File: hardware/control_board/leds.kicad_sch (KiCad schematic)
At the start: 18 parts, among them Q1 PMV450ENEA

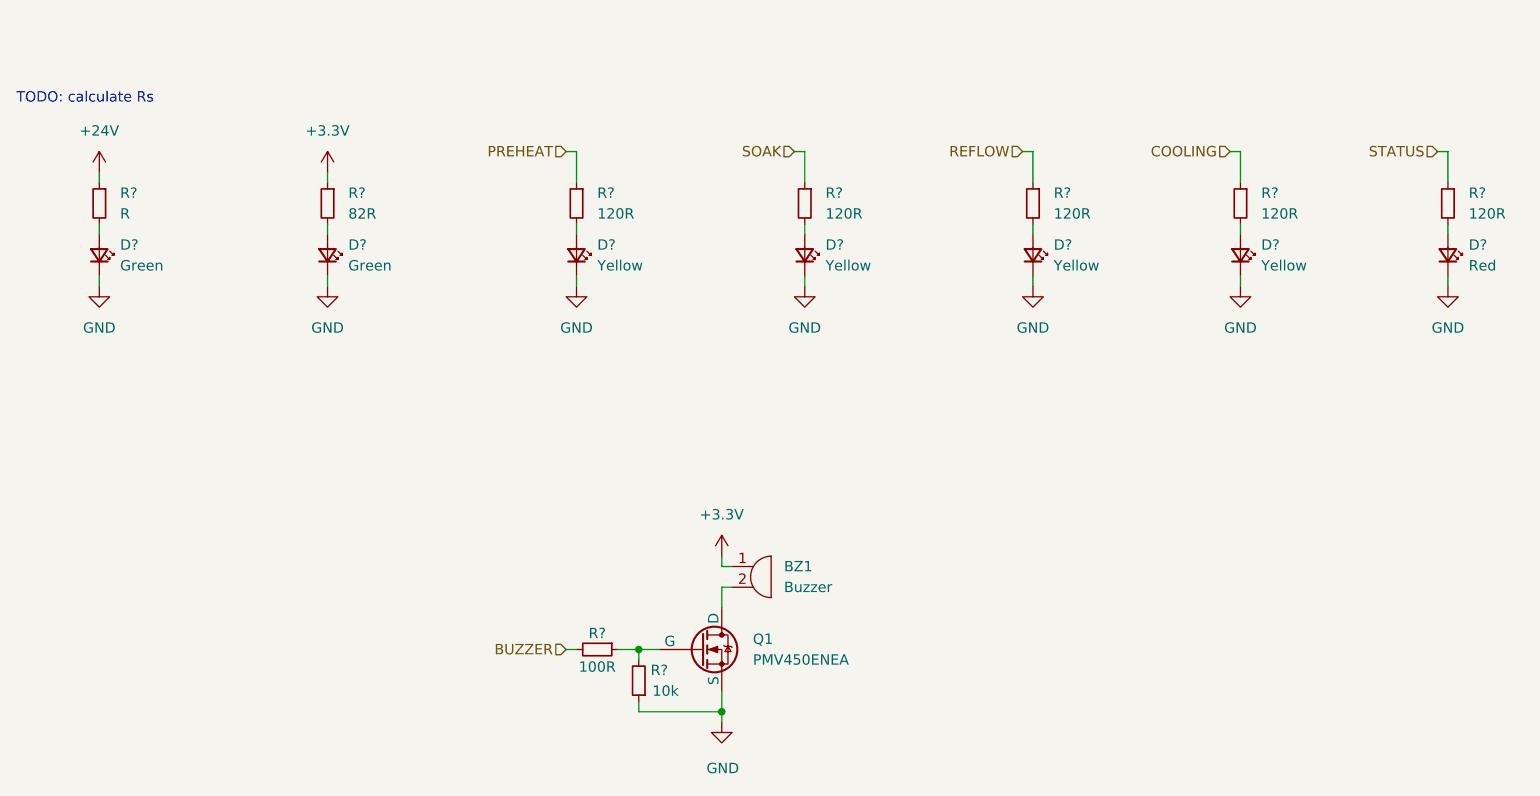
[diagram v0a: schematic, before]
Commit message: Adjust component values
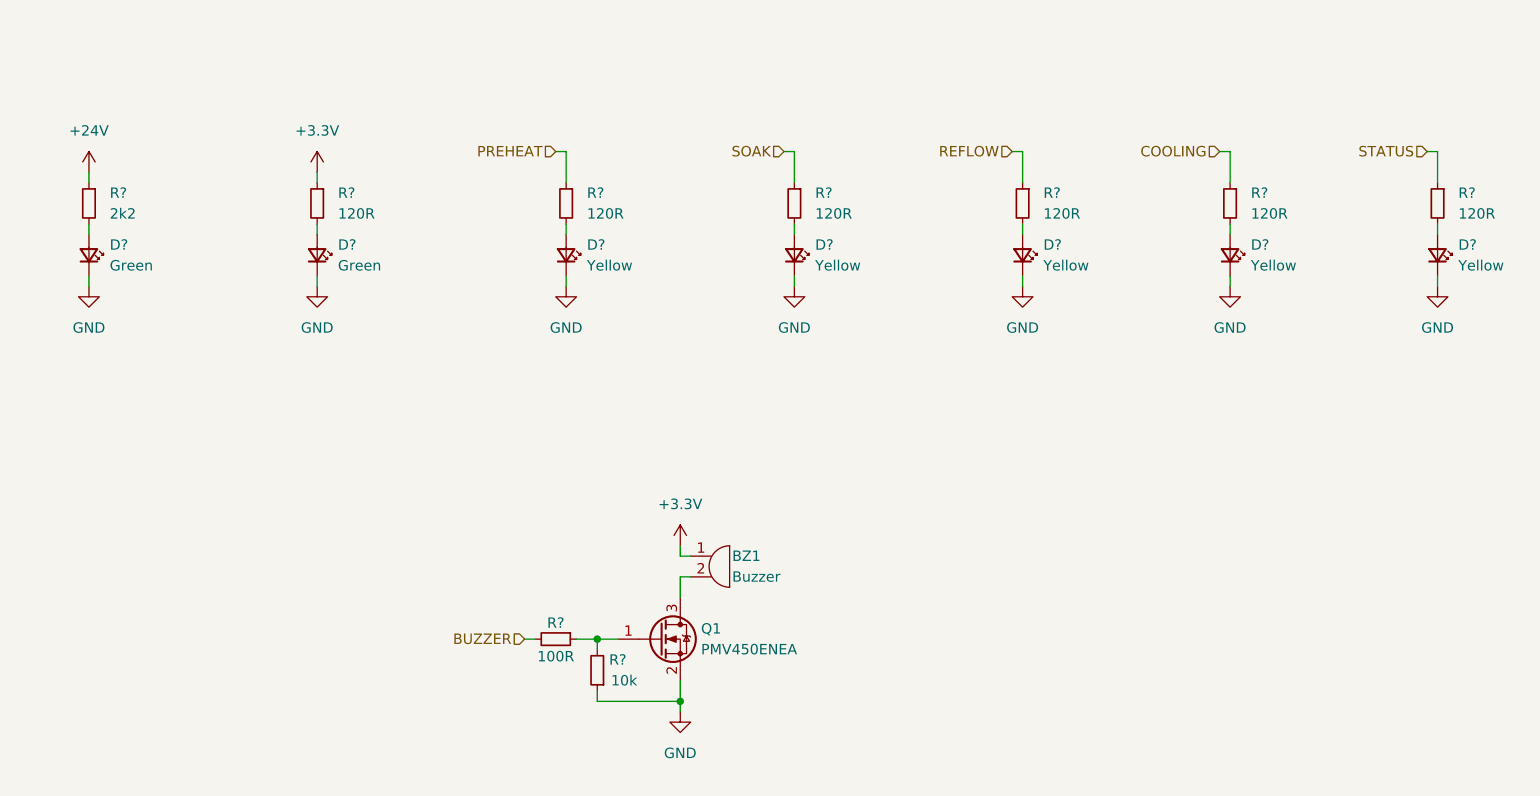
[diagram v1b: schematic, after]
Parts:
- removed Q1: PMV450ENEA, symbol Simulation_SPICE:NMOS
- added Q1: PMV450ENEA, Package_TO_SOT_SMD:SOT-23, symbol Device:Q_NMOS_GSD
- BZ1: footprint Buzzer_Beeper:Buzzer_12x9.5RM7.6 -> Local_Library:PKM13EPYH4000-A0
- D?: value Red -> Yellow
- R?: value 82R -> 120R
- R?: value R -> 2k2
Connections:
- net GND: now also Q1.2 (S)
- net at BZ1.2: now also Q1.3 (D)
- net at R?.1, R?.2: now also Q1.1 (G)
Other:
- note removed: "TODO: calculate Rs"
- moved on the sheet: BZ1, D?, R?

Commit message: Assign footprints to components
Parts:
- removed Q1: PMV450ENEA, Package_TO_SOT_SMD:SOT-23, symbol Device:Q_NMOS_GSD
- added Q1: 2N7002A, Package_TO_SOT_SMD:SOT-23, symbol Transistor_FET:2N7002
- BZ1: Component (none) -> PKM13EPYH4000-A0
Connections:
- net GND: now also Q1.2 (S)
- net at BZ1.2: now also Q1.3 (D)
- net at R?.1, R?.2: now also Q1.1 (G)
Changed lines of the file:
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@@
   (title_block
     (title "LED & Buzzer")
-    (date "2023-07-22")
+    (date "2023-07-29")
     (rev "${REVISION}")
     (company "Author: I. Kajdan")
@@
         )
         (path "/b652b05a-4e3d-4ad1-b032-18886abe7d45/1df5b500-a950-4c3c-8279-0c408859e423"
-          (reference "#PWR056") (unit 1)
+          (reference "#PWR057") (unit 1)
         )
       )
@@
         )
         (path "/b652b05a-4e3d-4ad1-b032-18886abe7d45/1df5b500-a950-4c3c-8279-0c408859e423"
-          (reference "#PWR057") (unit 1)
+          (reference "#PWR058") (unit 1)
         )
       )
@@
   (symbol (lib_id "PKM13EPYH4000-A0:PKM13EPYH4000-A0") (at 142.24 135.89 0) (unit 1)
     (in_bom yes) (on_board yes) (dnp no)
-    (property "Reference" "BZ1" (at 144.78 134.62 0)
-      (effects (font (size 1.27 1.27)) (justify left))
-    )
-    (property "Value" "Buzzer" (at 144.78 137.16 0)
+    (property "Reference" "BZ1" (at 145.415 134.62 0)
+      (effects (font (size 1.27 1.27)) (justify left))
+    )
+    (property "Value" "Buzzer" (at 145.415 137.16 0)
       (effects (font (size 1.27 1.27)) (justify left))
     )
@@
       (effects (font (size 1.27 1.27)) hide)
     )
+    (property "Component" "PKM13EPYH4000-A0" (at 142.24 135.89 0)
+      (effects (font (size 1.27 1.27)) hide)
+    )
     (pin "1")
     (pin "2")
@@
         )
         (path "/b652b05a-4e3d-4ad1-b032-18886abe7d45/1df5b500-a950-4c3c-8279-0c408859e423"
-          (reference "#PWR055") (unit 1)
+          (reference "#PWR056") (unit 1)
         )
       )
@@
         )
         (path "/b652b05a-4e3d-4ad1-b032-18886abe7d45/1df5b500-a950-4c3c-8279-0c408859e423"
-          (reference "#PWR049") (unit 1)
+          (reference "#PWR050") (unit 1)
         )
       )
@@
         )
         (path "/b652b05a-4e3d-4ad1-b032-18886abe7d45/1df5b500-a950-4c3c-8279-0c408859e423"
-          (reference "#PWR054") (unit 1)
+          (reference "#PWR055") (unit 1)
         )
       )
@@
         )
         (path "/b652b05a-4e3d-4ad1-b032-18886abe7d45/1df5b500-a950-4c3c-8279-0c408859e423"
-          (reference "#PWR048") (unit 1)
+          (reference "#PWR049") (unit 1)
         )
       )
@@
         )
         (path "/b652b05a-4e3d-4ad1-b032-18886abe7d45/1df5b500-a950-4c3c-8279-0c408859e423"
-          (reference "#PWR050") (unit 1)
+          (reference "#PWR051") (unit 1)
         )
       )
@@
         )
         (path "/b652b05a-4e3d-4ad1-b032-18886abe7d45/1df5b500-a950-4c3c-8279-0c408859e423"
-          (reference "#PWR052") (unit 1)
-        )
-      )
-    )
-  )
-  (symbol (lib_id "Device:Q_NMOS_GSD") (at 135.89 144.78 0) (unit 1)
-    (in_bom yes) (on_board yes) (dnp no)
-    (property "Reference" "Q1" (at 140.97 143.51 0)
-      (effects (font (size 1.27 1.27)) (justify left))
-    )
-    (property "Value" "PMV450ENEA" (at 140.97 146.05 0)
-      (effects (font (size 1.27 1.27)) (justify left))
-    )
-    (property "Footprint" "Package_TO_SOT_SMD:SOT-23" (at 140.97 142.24 0)
-      (effects (font (size 1.27 1.27)) hide)
-    )
-    (property "Datasheet" "https://assets.nexperia.com/documents/data-sheet/PMV450ENEA.pdf" (at 135.89 144.78 0)
-      (effects (font (size 1.27 1.27)) hide)
-    )
-    (pin "1")
-    (pin "2")
-    (pin "3")
-    (instances
-      (project "control_board"
-        (path "/b652b05a-4e3d-4ad1-b032-18886abe7d45/1df5b500-a950-4c3c-8279-0c408859e423"
-          (reference "Q1") (unit 1)
+          (reference "#PWR053") (unit 1)
         )
       )
@@
         )
         (path "/b652b05a-4e3d-4ad1-b032-18886abe7d45/1df5b500-a950-4c3c-8279-0c408859e423"
-          (reference "#PWR051") (unit 1)
+          (reference "#PWR052") (unit 1)
         )
       )
@@
         )
         (path "/b652b05a-4e3d-4ad1-b032-18886abe7d45/1df5b500-a950-4c3c-8279-0c408859e423"
-          (reference "#PWR047") (unit 1)
+          (reference "#PWR048") (unit 1)
         )
       )
@@
         )
         (path "/b652b05a-4e3d-4ad1-b032-18886abe7d45/1df5b500-a950-4c3c-8279-0c408859e423"
-          (reference "#PWR053") (unit 1)
+          (reference "#PWR054") (unit 1)
         )
       )
@@
         )
       )
+    )
+  )
+  (symbol (lib_id "Transistor_FET:2N7002") (at 135.89 144.78 0) (unit 1)
+    (in_bom yes) (on_board yes) (dnp no)
+    (property "Reference" "Q1" (at 140.97 143.51 0)
+      (effects (font (size 1.27 1.27)) (justify left))
+    )
+    (property "Value" "2N7002A" (at 140.97 146.05 0)
+      (effects (font (size 1.27 1.27)) (justify left))
+    )
+    (property "Footprint" "Package_TO_SOT_SMD:SOT-23" (at 140.97 146.685 0)
+      (effects (font (size 1.27 1.27) italic) (justify left) hide)
+    )
+    (property "Datasheet" "https://www.onsemi.com/pub/Collateral/NDS7002A-D.PDF" (at 135.89 144.78 0)
+      (effects (font (size 1.27 1.27)) (justify left) hide)
+    )
+    (pin "1")
+    (pin "2")
+    (pin "3")
+    (instances
+      (project "control_board"
+        (path "/b652b05a-4e3d-4ad1-b032-18886abe7d45/1df5b500-a950-4c3c-8279-0c408859e423"
+          (reference "Q1") (unit 1)
+        )
+      )

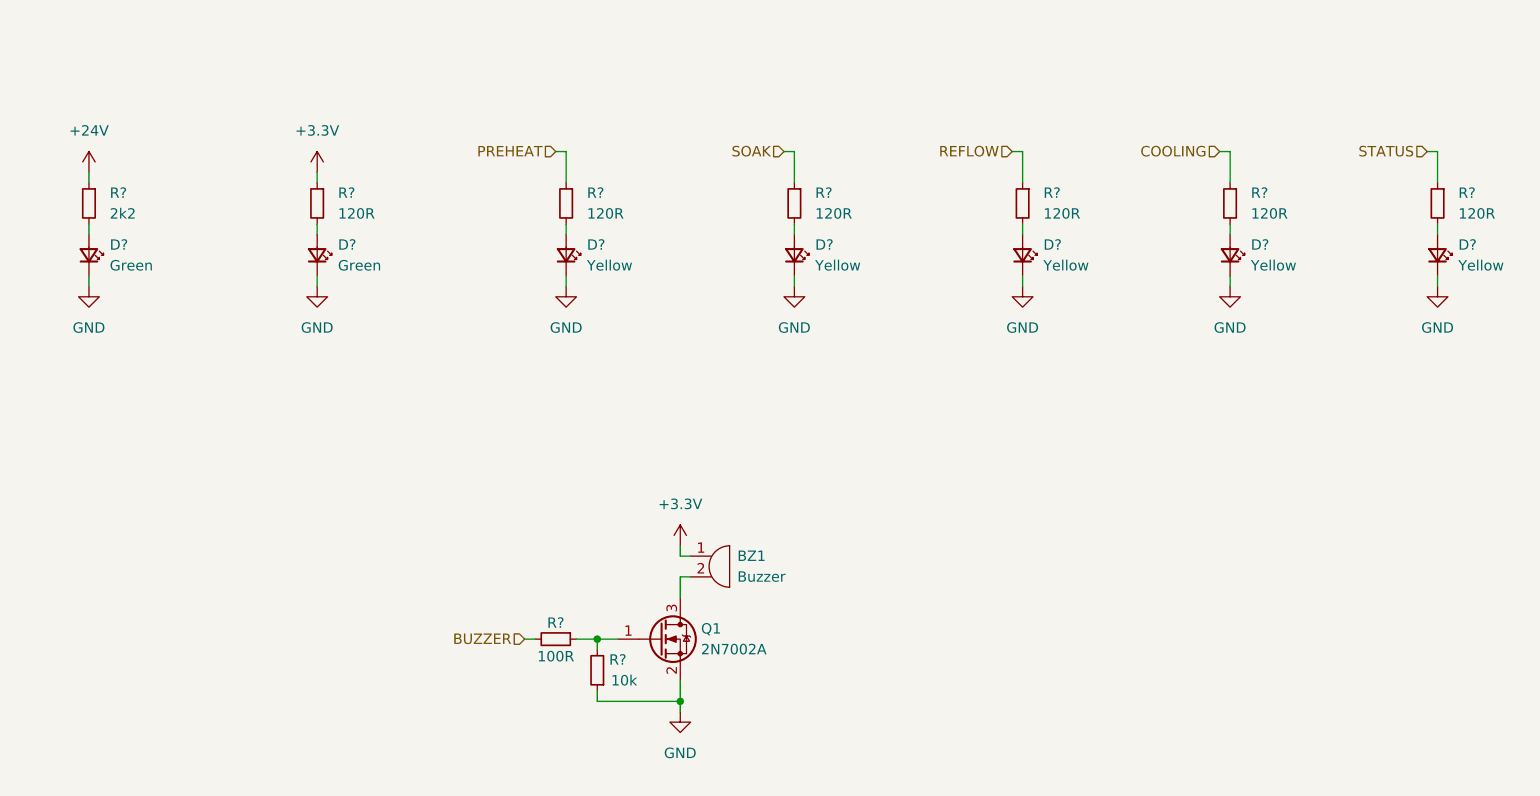
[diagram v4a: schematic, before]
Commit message: Route control board PCB tracks
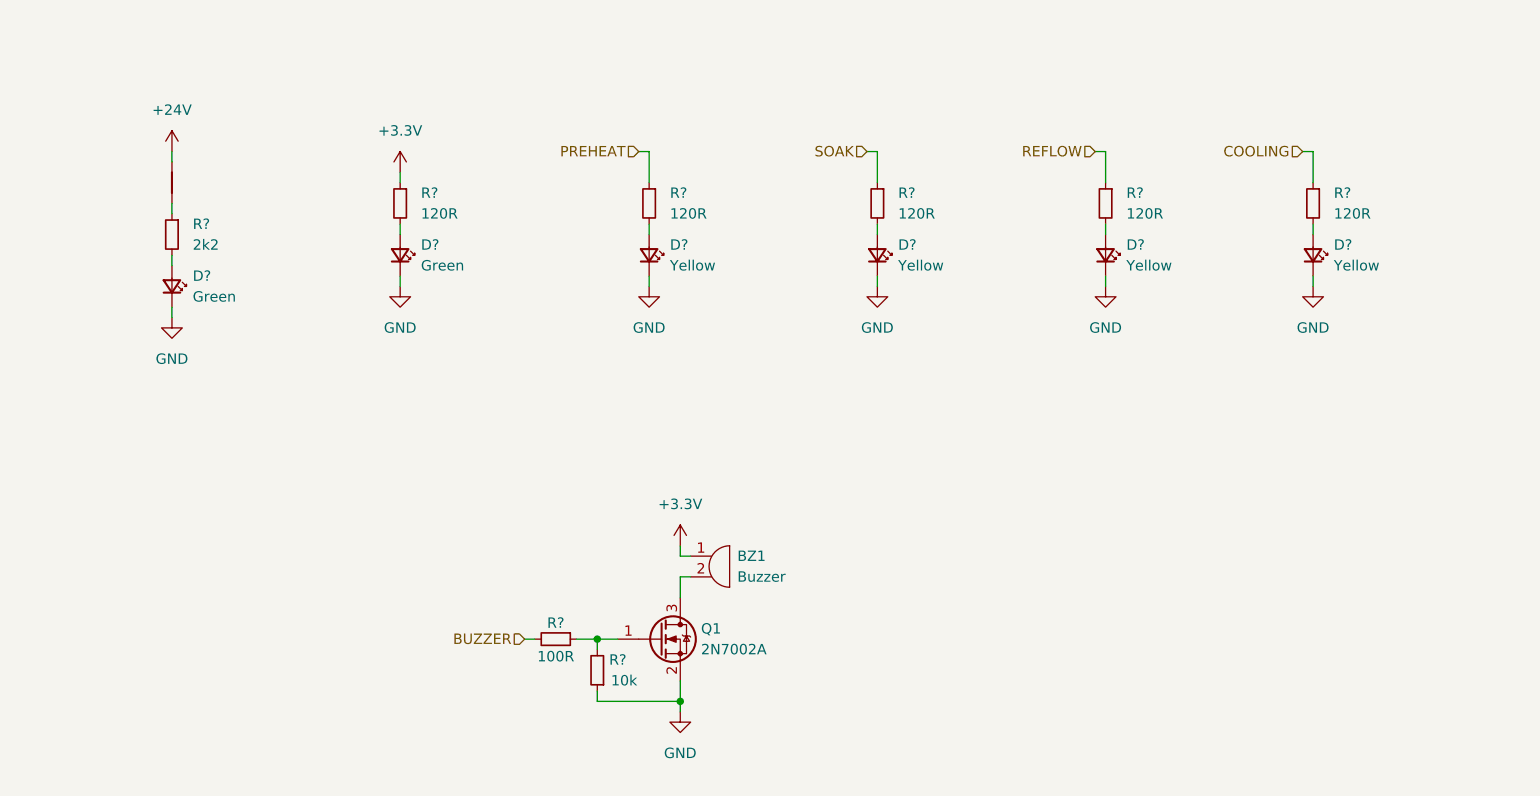
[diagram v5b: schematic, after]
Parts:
- removed D?: Yellow, LED_SMD:LED_0603_1608Metric, symbol Device:LED_Small
- removed R?: 120R, Resistor_SMD:R_0603_1608Metric, symbol Device:R_Small
- added NT1: NetTie_2, Local_Library:NetTie-2_SMD_Pad0.2mm, symbol Device:NetTie_2
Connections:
- net +24V: now also NT1.2; no longer R?.1
- new net: NT1.1, R?.1
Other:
- moved on the sheet: D?, R?

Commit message: Cleanup the project
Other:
- moved on the sheet: BZ1, D?, Q1, R?
